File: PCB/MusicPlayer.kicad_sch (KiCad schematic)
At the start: 22 parts, among them J1 Conn_ST_STDC14, J2 Conn_01x02, J3 USB_C_Receptacle_USB2.0_16P, SW1 Reset, SW2 RotaryEncoder, U1 STM32G031K8U6, U2 MAX17048G, U3 MCP73831-2-OT, U4 AMS1117-3.3, U5 CH340C, U6 USBLC6-2SC6

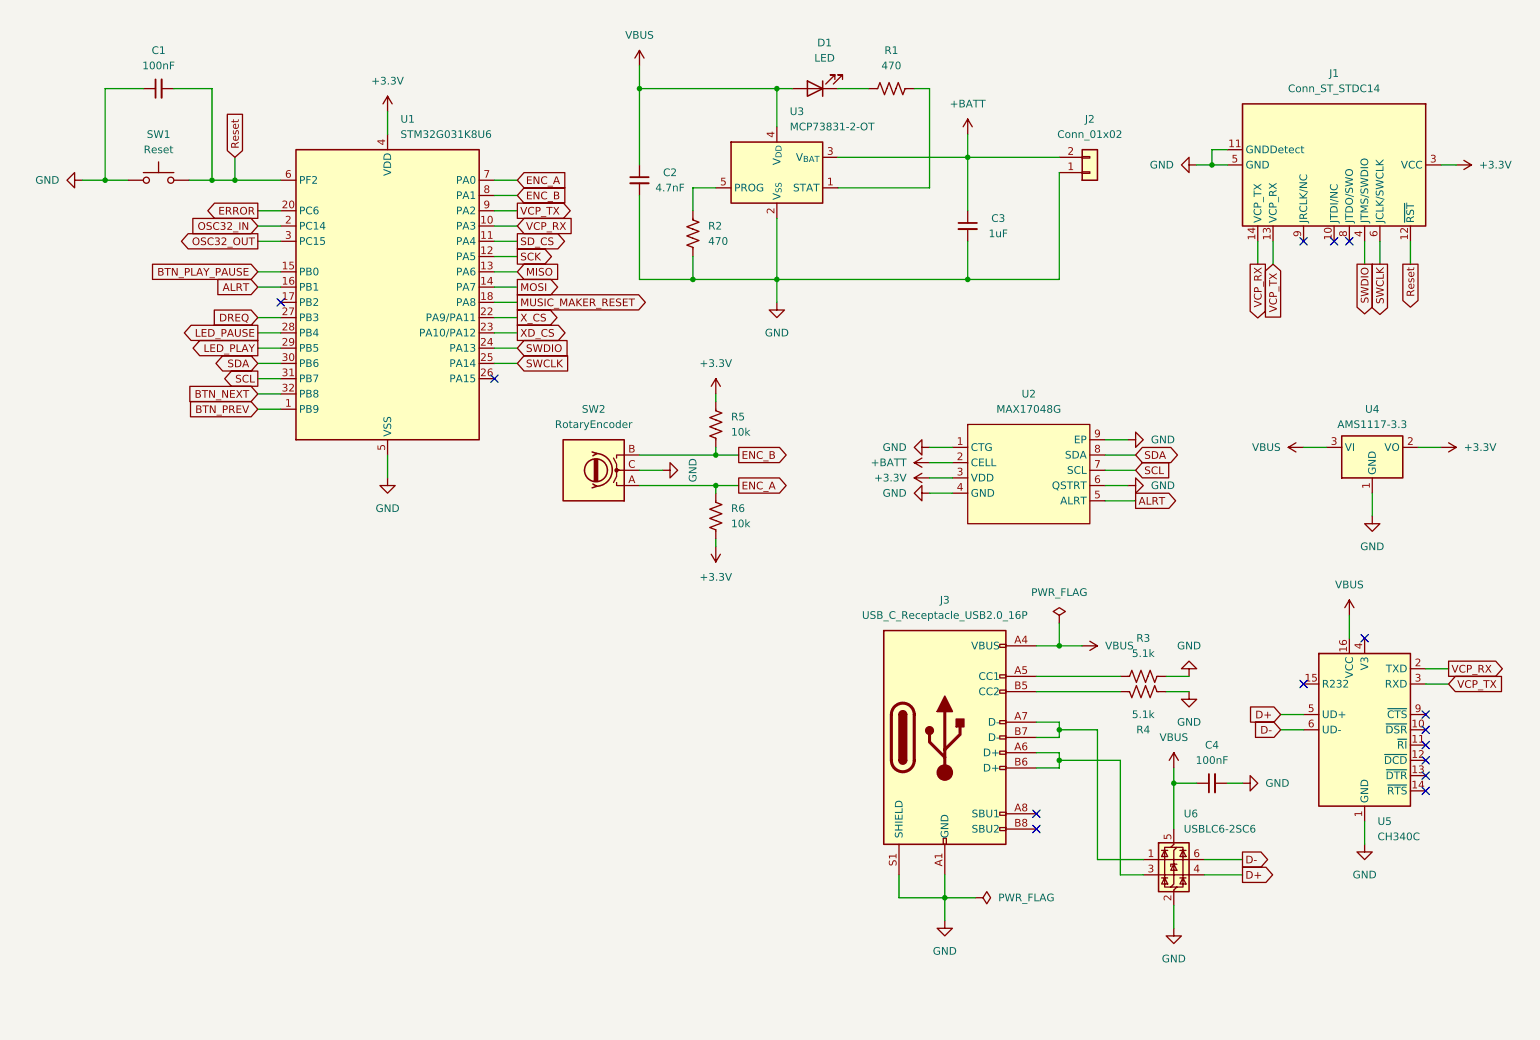
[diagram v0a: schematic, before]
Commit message: Add Music Maker FeatherWing symbol and update schematic
Replaced a capacitor symbol with a new custom symbol for the Adafruit Music Maker FeatherWing in the schematic, including pin definitions and properties. Updated the project and symbol cache files accordingly. Also rotated backup files, removing old ones and adding new backups.
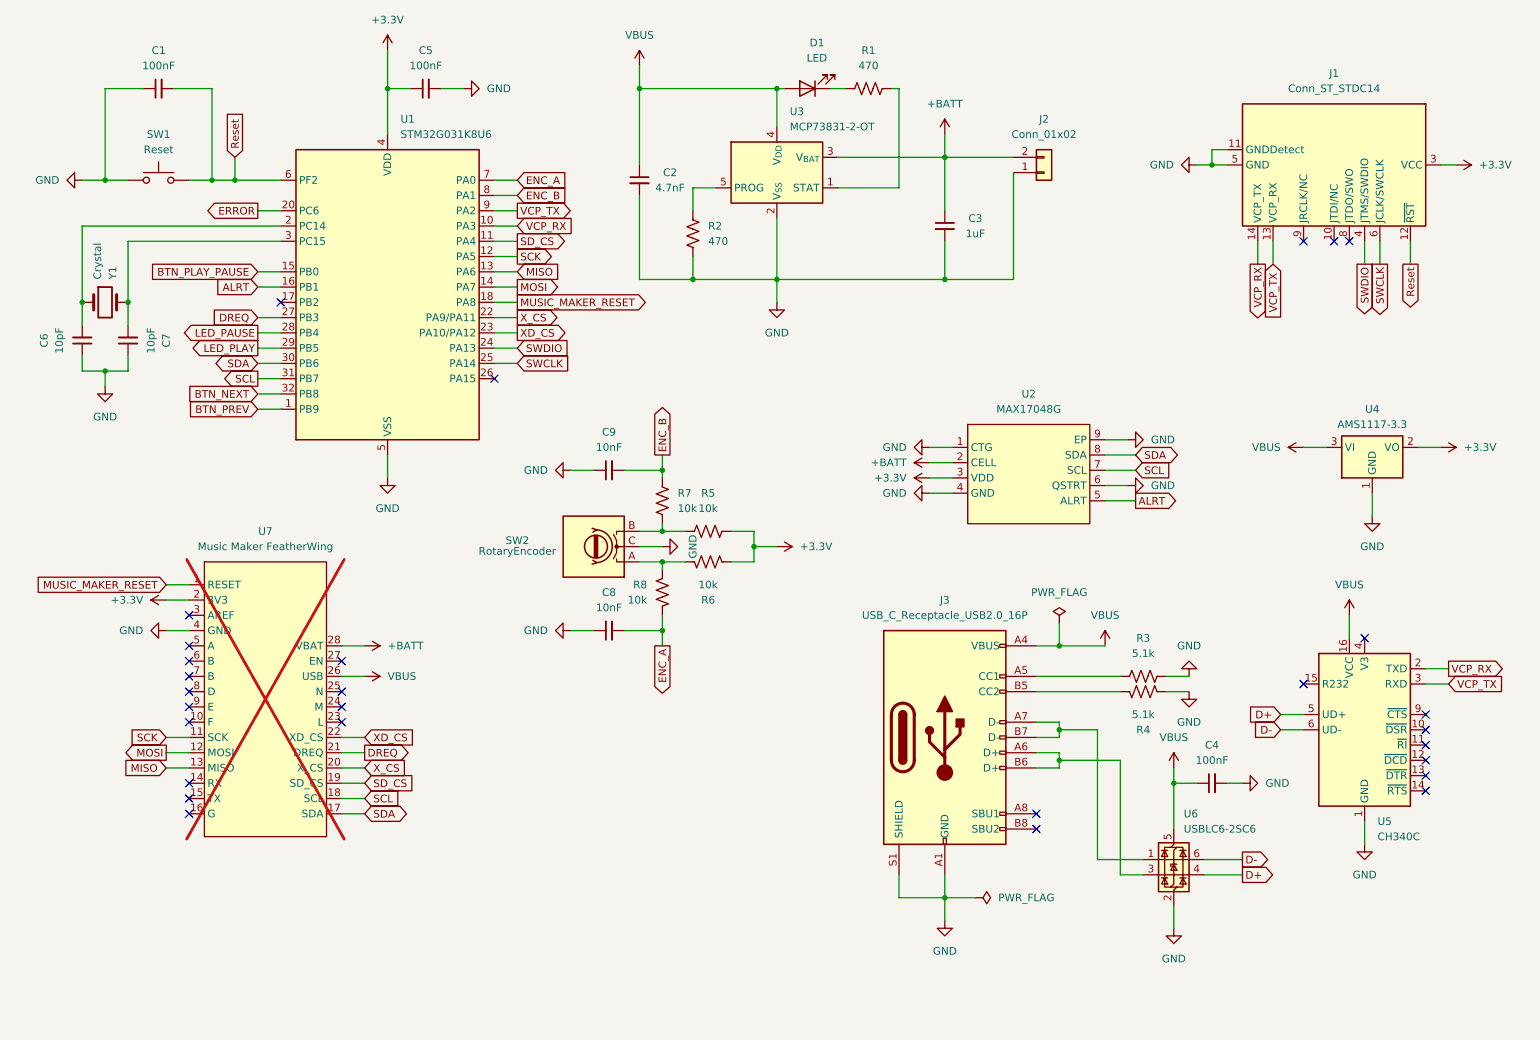
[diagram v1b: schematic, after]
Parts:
- added C5: 100nF, Capacitor_SMD:C_0603_1608Metric, symbol Device:C_Small
- added C6, C7: 10pF, Capacitor_SMD:C_0603_1608Metric, symbol Device:C_Small
- added C8, C9: 10nF, Capacitor_SMD:C_0603_1608Metric, symbol Device:C_Small
- added R7, R8: 10k, symbol Device:R_US
- added U7: Music Maker FeatherWing, CustomFootprints:Music_Maker_Feather_Wing, symbol CustomSymbols:Music_Maker_FeatherWing
- added Y1: Crystal, symbol Device:Crystal
- SW2: footprint (none) -> Rotary_Encoder:RotaryEncoder_Alps_EC11E_Vertical_H20mm; LSCS (none) -> C470709
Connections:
- net +3.3V: now also R5.1, C5.1, U7.2 (3V3); no longer R5.2
- net +BATT: now also U7.28 (VBAT)
- net DREQ: now also U7.21 (DREQ)
- net ENC_A: now also C8.2, R8.2; no longer R6.2, SW2.A
- net ENC_B: now also C9.2, R7.1; no longer R5.1, SW2.B
- net GND: now also C5.2, C6.1, C7.1, C8.1, C9.1, U7.4 (GND)
- net MISO: now also U7.13 (MISO)
- net MOSI: now also U7.12 (MOSI)
- net MUSIC_MAKER_RESET: now also U7.1 (RESET)
- net SCK: now also U7.11 (SCK)
- net SCL: now also U7.18 (SCL)
- net SDA: now also U7.17 (SDA)
- net SD_CS: now also U7.19 (SD_CS)
- net VBUS: now also U7.26 (USB)
- net XD_CS: now also U7.22 (XD_CS)
- net X_CS: now also U7.20 (X_CS)
- net OSC32_IN: no longer names the net of U1.2 (PC14)
- net OSC32_IN: now also C6.2, Y1.1
- net OSC32_OUT: no longer names the net of U1.3 (PC15)
- net OSC32_OUT: now also C7.2, Y1.2
- new net: R6.2, R8.1, SW2.A
- new net: R5.2, R7.2, SW2.B
- no-connect marks 15 -> 29
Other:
- moved on the sheet: C3, D1, J2, R1, R5, R6, SW2

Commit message: Add input, output, power, and USB schematics
Added new KiCad schematic files for Inputs, Outputs, Power, and USB. Updated MusicPlayer PCB and schematic files, replaced old backup files with new ones, and added a new untitled schematic. These changes expand the project with additional schematic modules and update the main board design.
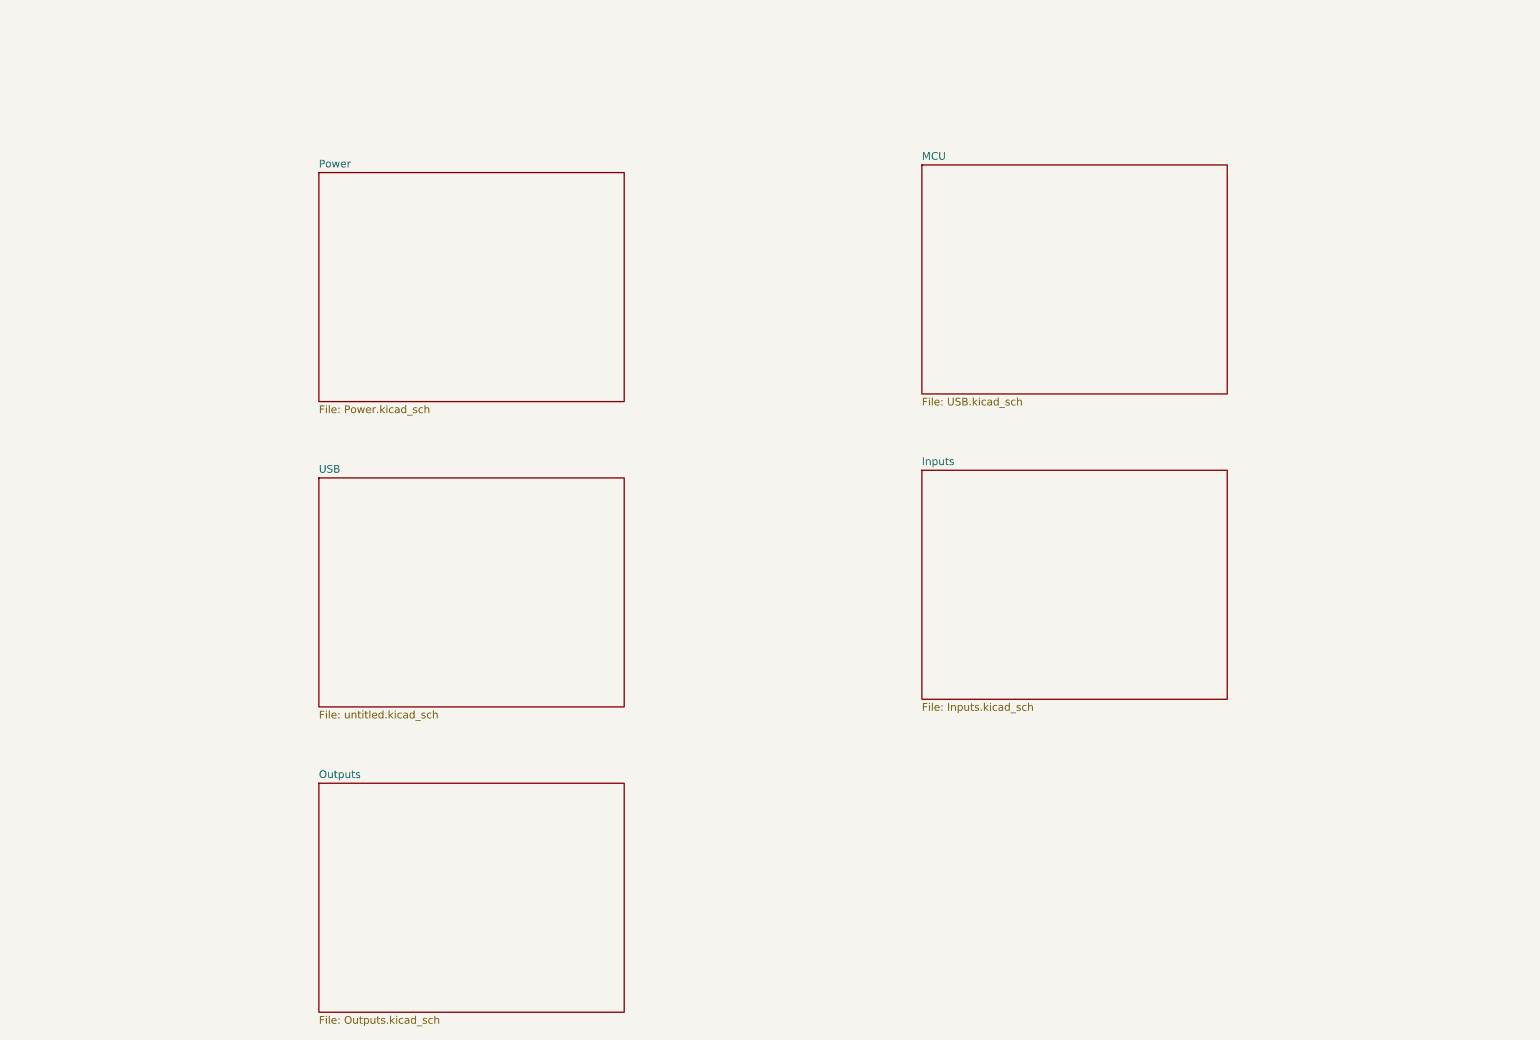
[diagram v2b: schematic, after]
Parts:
- removed C1, C4, C5: 100nF, Capacitor_SMD:C_0603_1608Metric, symbol Device:C_Small
- removed C2: 4.7nF, Capacitor_SMD:C_0603_1608Metric, symbol Device:C_Small
- removed C3: 1uF, Capacitor_SMD:C_0603_1608Metric, symbol Device:C_Small
- removed C6, C7: 10pF, Capacitor_SMD:C_0603_1608Metric, symbol Device:C_Small
- removed C8, C9: 10nF, Capacitor_SMD:C_0603_1608Metric, symbol Device:C_Small
- removed D1: LED, symbol Device:LED
- removed J1: Conn_ST_STDC14, Connector_PinHeader_1.27mm:PinHeader_2x07_P1.27mm_Vertical_SMD, symbol Connector:Conn_ST_STDC14
- removed J2: Conn_01x02, Connector_JST:JST_PH_S2B-PH-K_1x02_P2.00mm_Horizontal, symbol Connector_Generic:Conn_01x02
- removed J3: USB_C_Receptacle_USB2.0_16P, Connector_USB:USB_C_Receptacle_G-Switch_GT-USB-7010ASV, symbol Connector:USB_C_Receptacle_USB2.0_16P
- removed R1, R2: 470, symbol Device:R_US
- removed R3, R4: 5.1k, symbol Device:R_US
- removed R5, R6, R7, R8: 10k, symbol Device:R_US
- removed SW1: Reset, Button_Switch_SMD:SW_SPST_TS-1088-xR020, symbol Switch:SW_Push
- removed SW2: RotaryEncoder, Rotary_Encoder:RotaryEncoder_Alps_EC11E_Vertical_H20mm, symbol Device:RotaryEncoder
- removed U1: STM32G031K8U6, Package_DFN_QFN:QFN-32-1EP_5x5mm_P0.5mm_EP3.45x3.45mm, symbol MCU_ST_STM32G0:STM32G031K8Ux
- removed U2: MAX17048G, Package_DFN_QFN:TDFN-8-1EP_2x2mm_P0.5mm_EP0.8x1.2mm, symbol CustomSymbols:MAX17048G
- removed U3: MCP73831-2-OT, Package_TO_SOT_SMD:SOT-23-5, symbol Battery_Management:MCP73831-2-OT
- removed U4: AMS1117-3.3, Package_TO_SOT_SMD:SOT-223-3_TabPin2, symbol Regulator_Linear:AMS1117-3.3
- removed U5: CH340C, Package_SO:SOIC-16_3.9x9.9mm_P1.27mm, symbol Interface_USB:CH340C
- removed U6: USBLC6-2SC6, Package_TO_SOT_SMD:SOT-23-6, symbol Power_Protection:USBLC6-2SC6
- removed U7: Music Maker FeatherWing, CustomFootprints:Music_Maker_Feather_Wing, symbol CustomSymbols:Music_Maker_FeatherWing
- removed Y1: Crystal, symbol Device:Crystal
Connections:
- no-connect marks 29 -> 0
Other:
- added sheet Inputs (Inputs.kicad_sch)
- added sheet MCU (USB.kicad_sch)
- added sheet Outputs (Outputs.kicad_sch)
- added sheet Power (Power.kicad_sch)
- added sheet USB (untitled.kicad_sch)

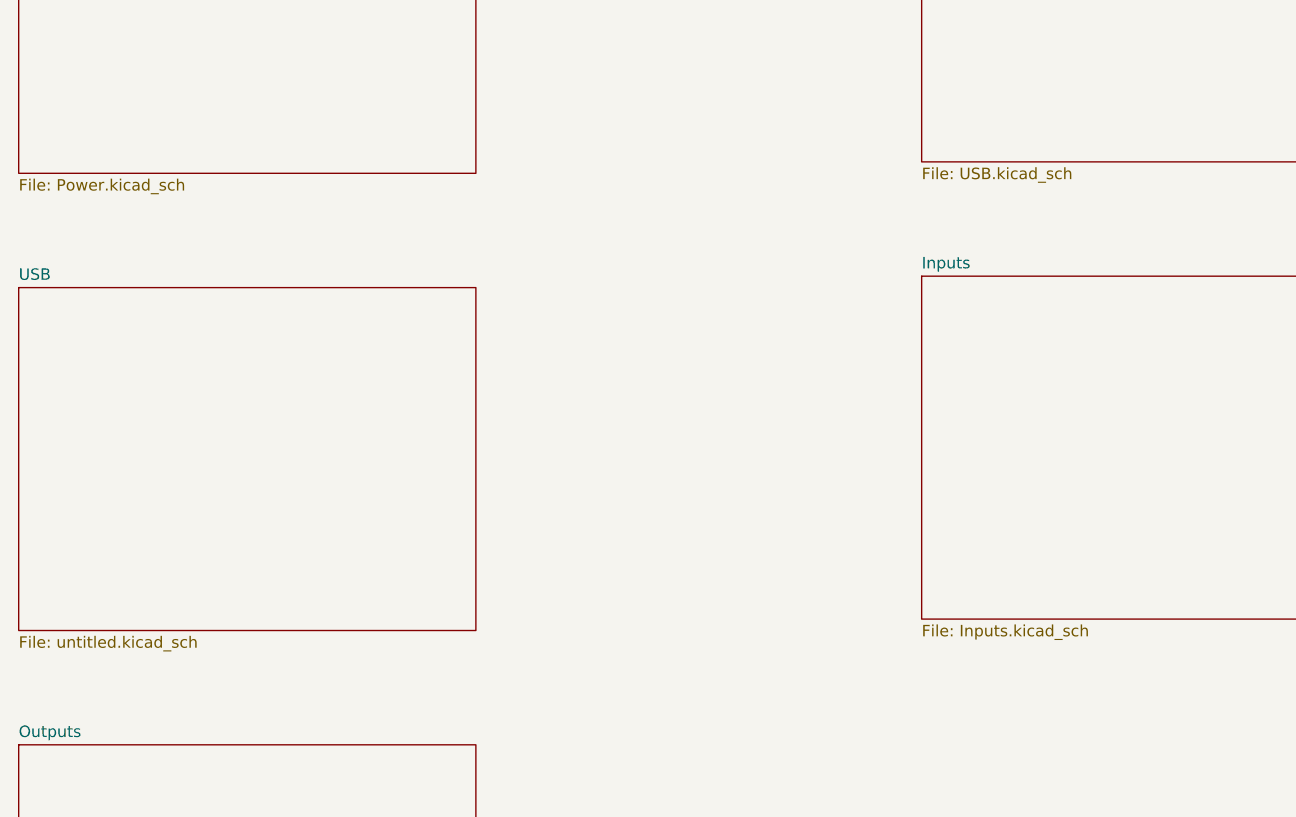
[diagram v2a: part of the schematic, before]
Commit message: Restarted the schematic
It was getting way to full.
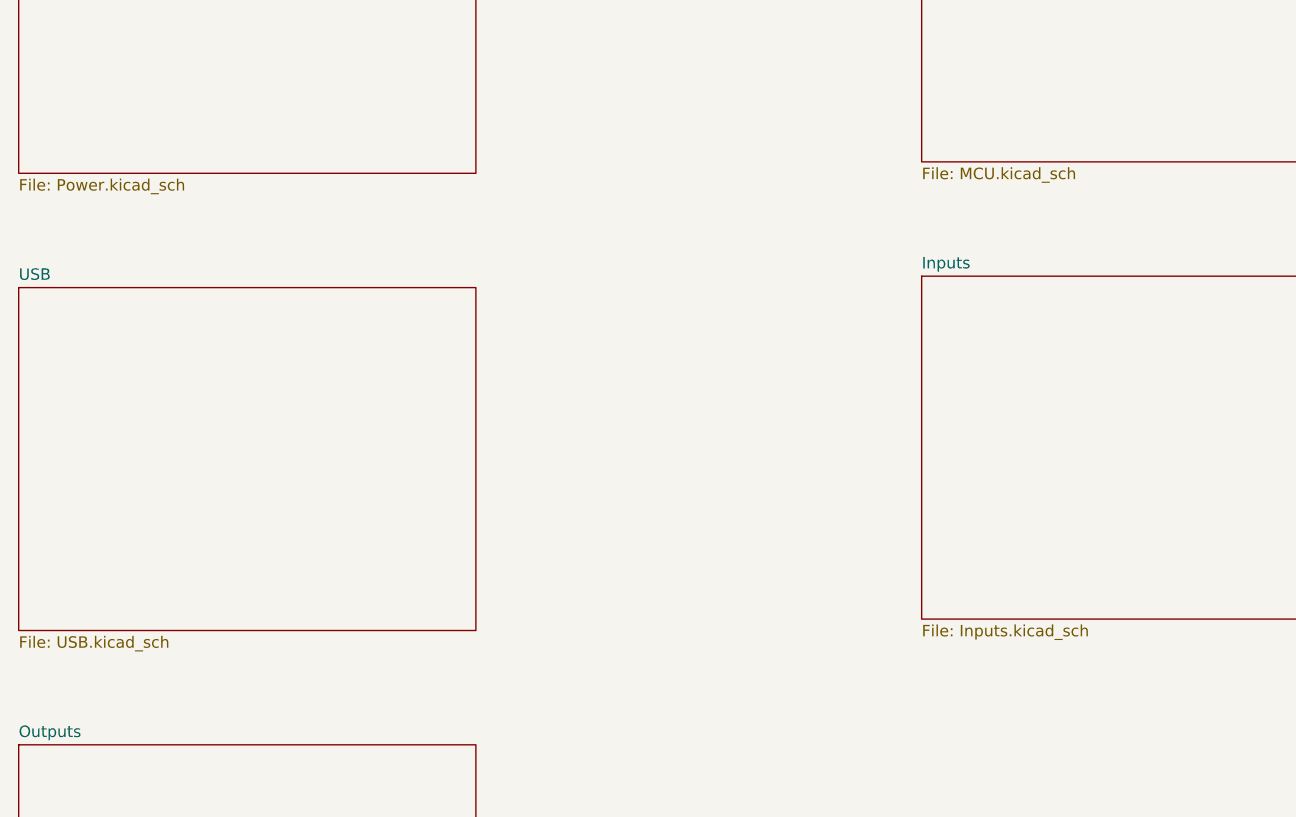
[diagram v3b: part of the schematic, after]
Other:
- sheet MCU: file USB.kicad_sch -> MCU.kicad_sch
- sheet USB: file untitled.kicad_sch -> USB.kicad_sch
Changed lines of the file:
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@@
 			)
 		)
-		(property "Sheetfile" "USB.kicad_sch"
+		(property "Sheetfile" "MCU.kicad_sch"
 			(at 161.29 76.7846 0)
 			(effects
@@
 			(project "MusicPlayer"
 				(path "/2c2d2da5-7991-4e93-87f2-9633b55e39cf"
-					(page "5")
+					(page "4")
 				)
 			)
@@
 			)
 		)
-		(property "Sheetfile" "untitled.kicad_sch"
+		(property "Sheetfile" "USB.kicad_sch"
 			(at 60.96 128.8546 0)
 			(effects
@@
 			(project "MusicPlayer"
 				(path "/2c2d2da5-7991-4e93-87f2-9633b55e39cf"
-					(page "4")
+					(page "5")
 				)
 			)
